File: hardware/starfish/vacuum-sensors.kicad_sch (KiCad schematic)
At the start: 2 parts, among them U601 XGZP6857D

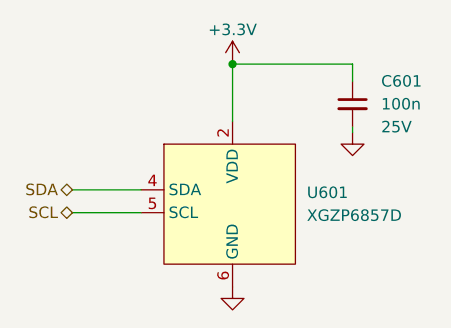
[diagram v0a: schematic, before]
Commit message: Mostly finished starfish schematic, ready for layout!
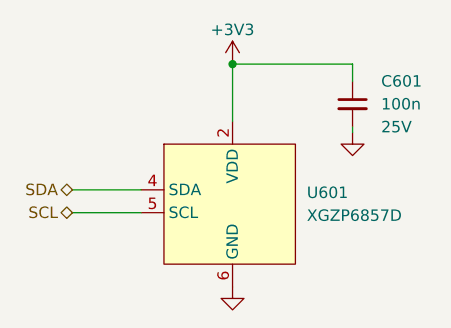
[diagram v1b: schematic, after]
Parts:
- C601: footprint Capacitor_SMD:C_0402_1005Metric_Pad0.74x0.62mm_HandSolder -> winterbloom:C_0402_HandSolder
- U601: mpn (none) -> XGZP6857D
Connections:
- net at U601.1 (NC): no longer U601.3 (NC)
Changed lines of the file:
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@@
       (effects (font (size 1.27 1.27)) (justify left))
     )
-    (property "Footprint" "Capacitor_SMD:C_0402_1005Metric_Pad0.74x0.62mm_HandSolder" (id 2) (at 154.94 96.52 0)
+    (property "Footprint" "winterbloom:C_0402_HandSolder" (id 2) (at 154.94 96.52 0)
       (effects (font (size 1.27 1.27)) hide)
     )
@@
     (pin "1")
     (pin "2")
-  )
-  (symbol (lib_id "power:+3.3V") (at 141.605 92.075 0) (unit 1)
-    (in_bom yes) (on_board yes) (fields_autoplaced)
-    (property "Reference" "#PWR0601" (id 0) (at 141.605 95.885 0)
-      (effects (font (size 1.27 1.27)) hide)
-    )
-    (property "Value" "+3.3V" (id 1) (at 141.605 88.265 0))
-    (property "Footprint" "" (id 2) (at 141.605 92.075 0)
-      (effects (font (size 1.27 1.27)) hide)
-    )
-    (property "Datasheet" "" (id 3) (at 141.605 92.075 0)
-      (effects (font (size 1.27 1.27)) hide)
-    )
-    (pin "1")
   )
   (symbol (lib_id "winterbloom:XGZP6857D") (at 141.605 107.315 0) (unit 1)
@@
       (effects (font (size 1.27 1.27)) hide)
     )
+    (property "mpn" "XGZP6857D" (id 4) (at 141.605 107.315 0)
+      (effects (font (size 1.27 1.27)) hide)
+    )
     (pin "1")
     (pin "2")
@@
     (pin "6")
   )
+  (symbol (lib_id "power:+3V3") (at 141.605 92.075 0) (unit 1)
+    (in_bom yes) (on_board yes)
+    (property "Reference" "#PWR0601" (id 0) (at 141.605 95.885 0)
+      (effects (font (size 1.27 1.27)) hide)
+    )
+    (property "Value" "+3V3" (id 1) (at 141.605 88.265 0))
+    (property "Footprint" "" (id 2) (at 141.605 92.075 0)
+      (effects (font (size 1.27 1.27)) hide)
+    )
+    (property "Datasheet" "" (id 3) (at 141.605 92.075 0)
+      (effects (font (size 1.27 1.27)) hide)
+    )
+    (pin "1")
+  )
 )
